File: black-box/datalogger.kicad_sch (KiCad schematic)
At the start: 75 parts, among them J1 RJ12, J10 PROG, J14 PWR, J4 Micro_SD_Card_Det1, J6 USB_C_Receptacle_USB2.0_16P, SW1 SW_SPST, U4 STM32F103C8Tx, U5 AP63200WU, U6 SN65HVD256D, U7 AP2204K-ADJ, Y1 8M, Y2 32.768k

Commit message: black-box: update
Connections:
- net GND: now also J10.3 (Pin_3)
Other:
- note added: "2025/12/30"
- note removed: "2025/12/25"
- moved on the sheet: C15, C16, C17, JP1, R21, R22, R5, TP11, TP12, TP13, TP14, U6

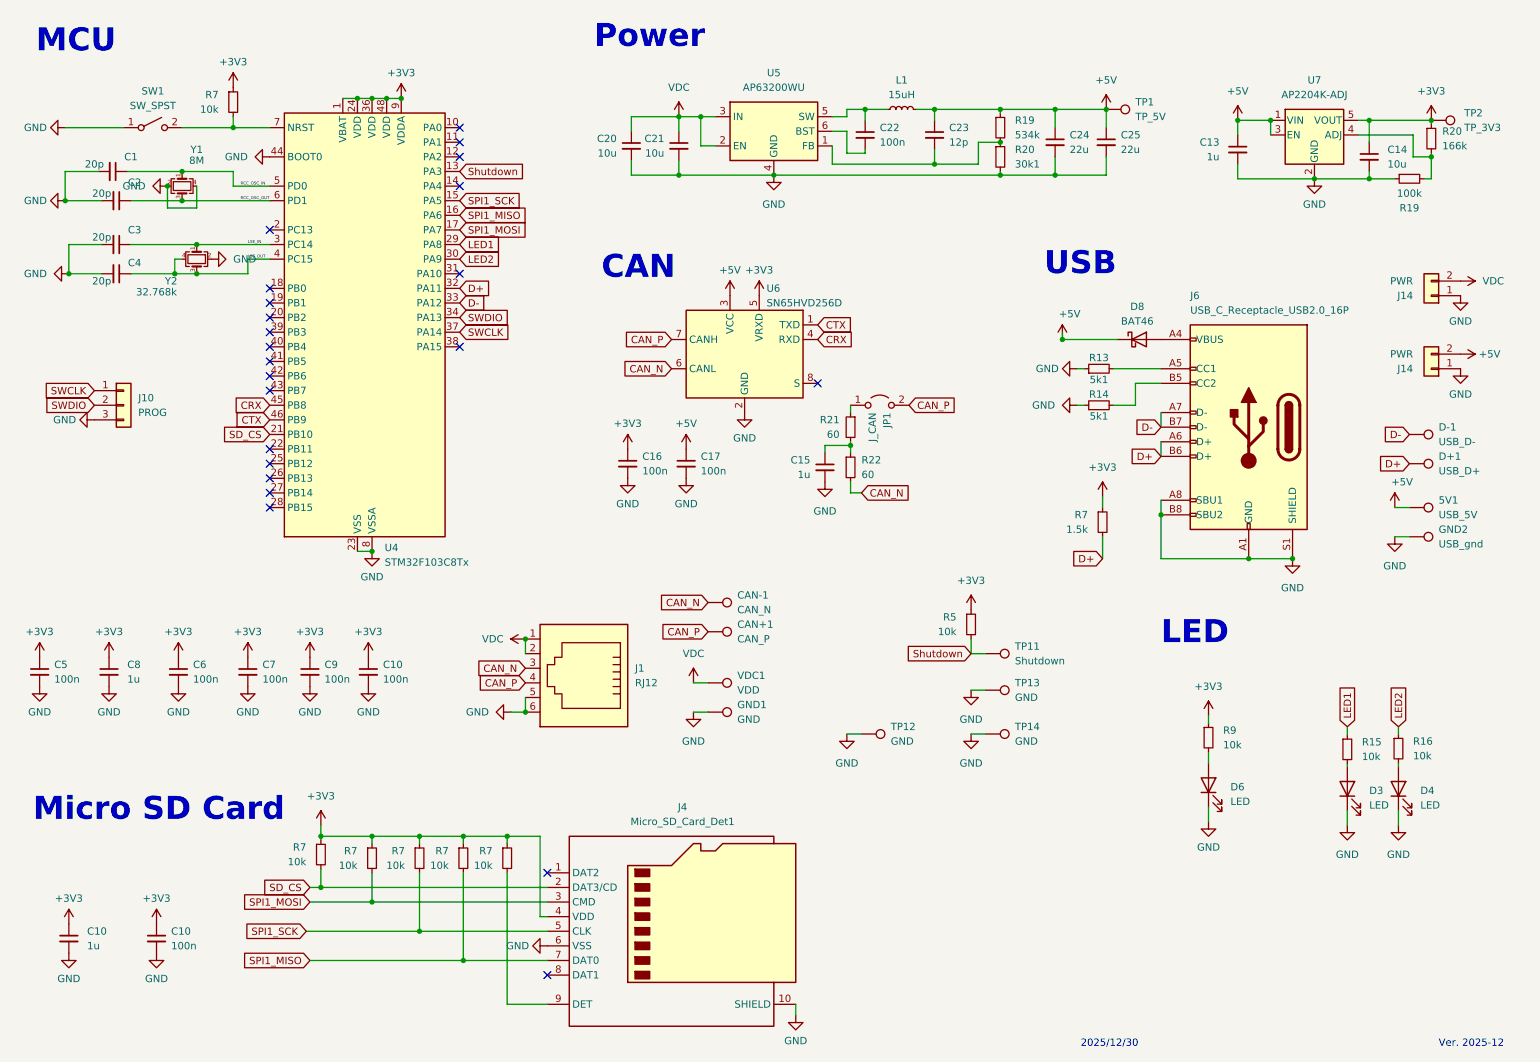
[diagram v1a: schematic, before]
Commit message: black-box: add WS2812 & 3D model
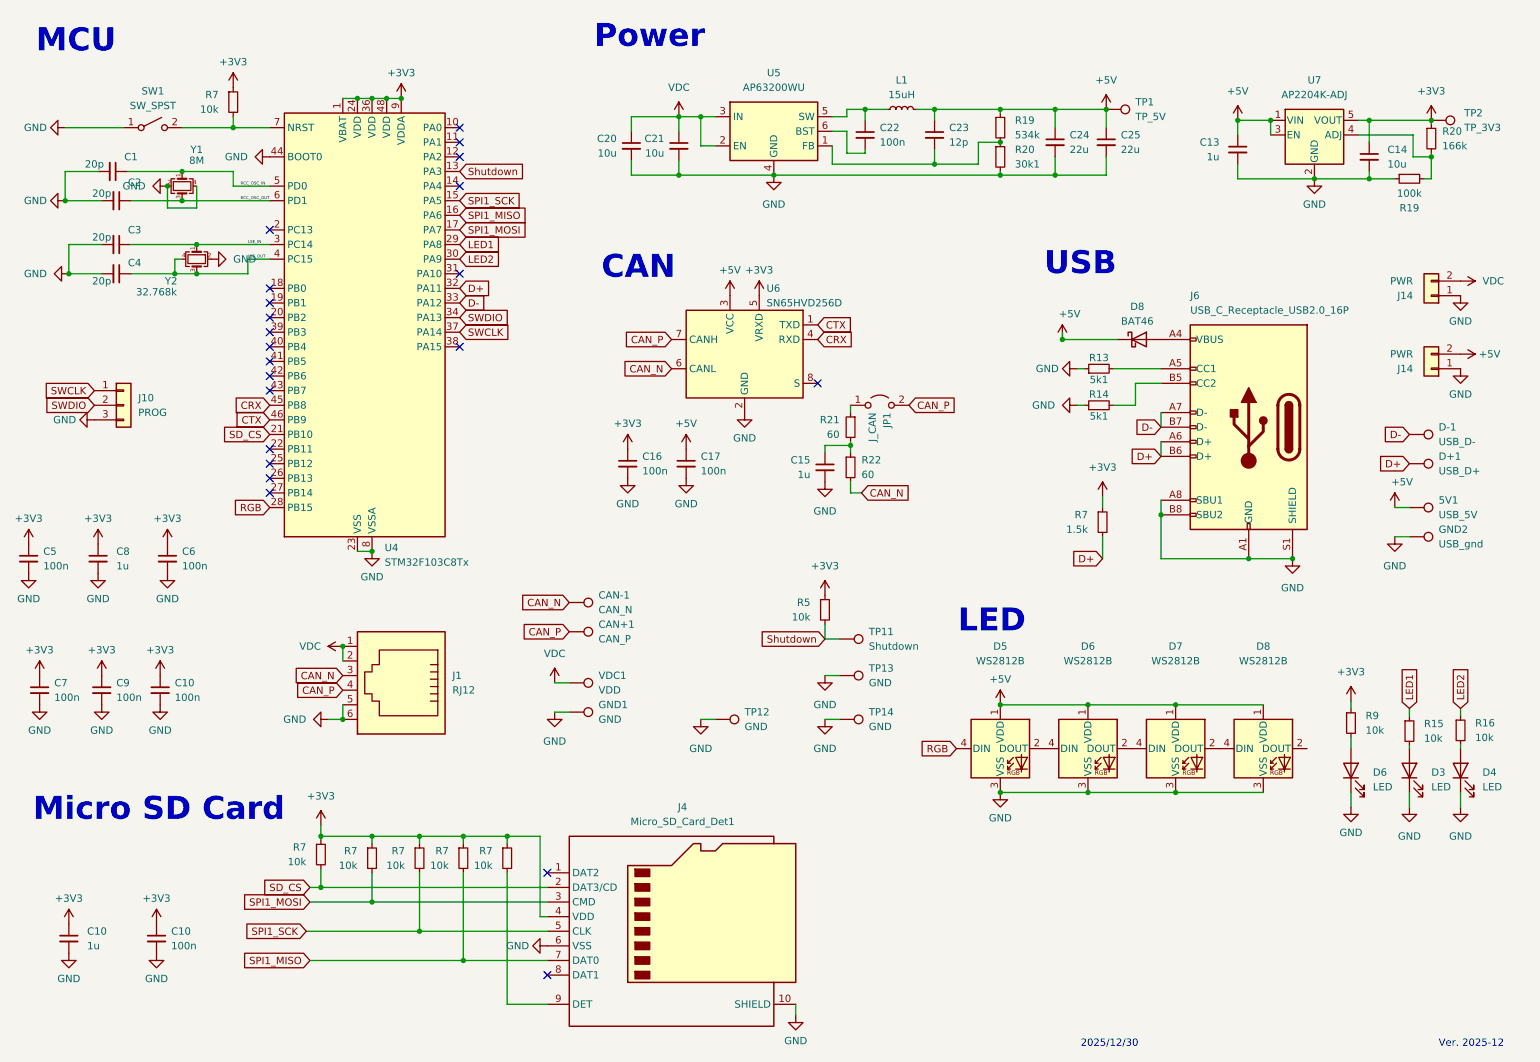
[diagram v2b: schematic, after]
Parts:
- added D5, D6, D7, D8: WS2812B, LED_SMD:LED_WS2812B_PLCC4_5.0x5.0mm_P3.2mm, symbol LED:WS2812B
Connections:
- net +5V: now also D5.1 (VDD), D6.1 (VDD), D7.1 (VDD), D8.1 (VDD)
- net GND: now also D5.3 (VSS), D6.3 (VSS), D7.3 (VSS), D8.3 (VSS)
- net RGB: now reaches U4.28 (PB15)
- net RGB: now also D5.4 (DIN)
- new net: D5.2 (DOUT), D6.4 (DIN)
- new net: D7.2 (DOUT), D8.4 (DIN)
- new net: D6.2 (DOUT), D7.4 (DIN)
- no-connect marks 23 -> 22
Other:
- moved on the sheet: C10, C5, C6, C7, C8, C9, CAN+1, CAN-1, D3, D4, D6, GND1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

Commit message: V2026.01: fix: USB pin and some issues
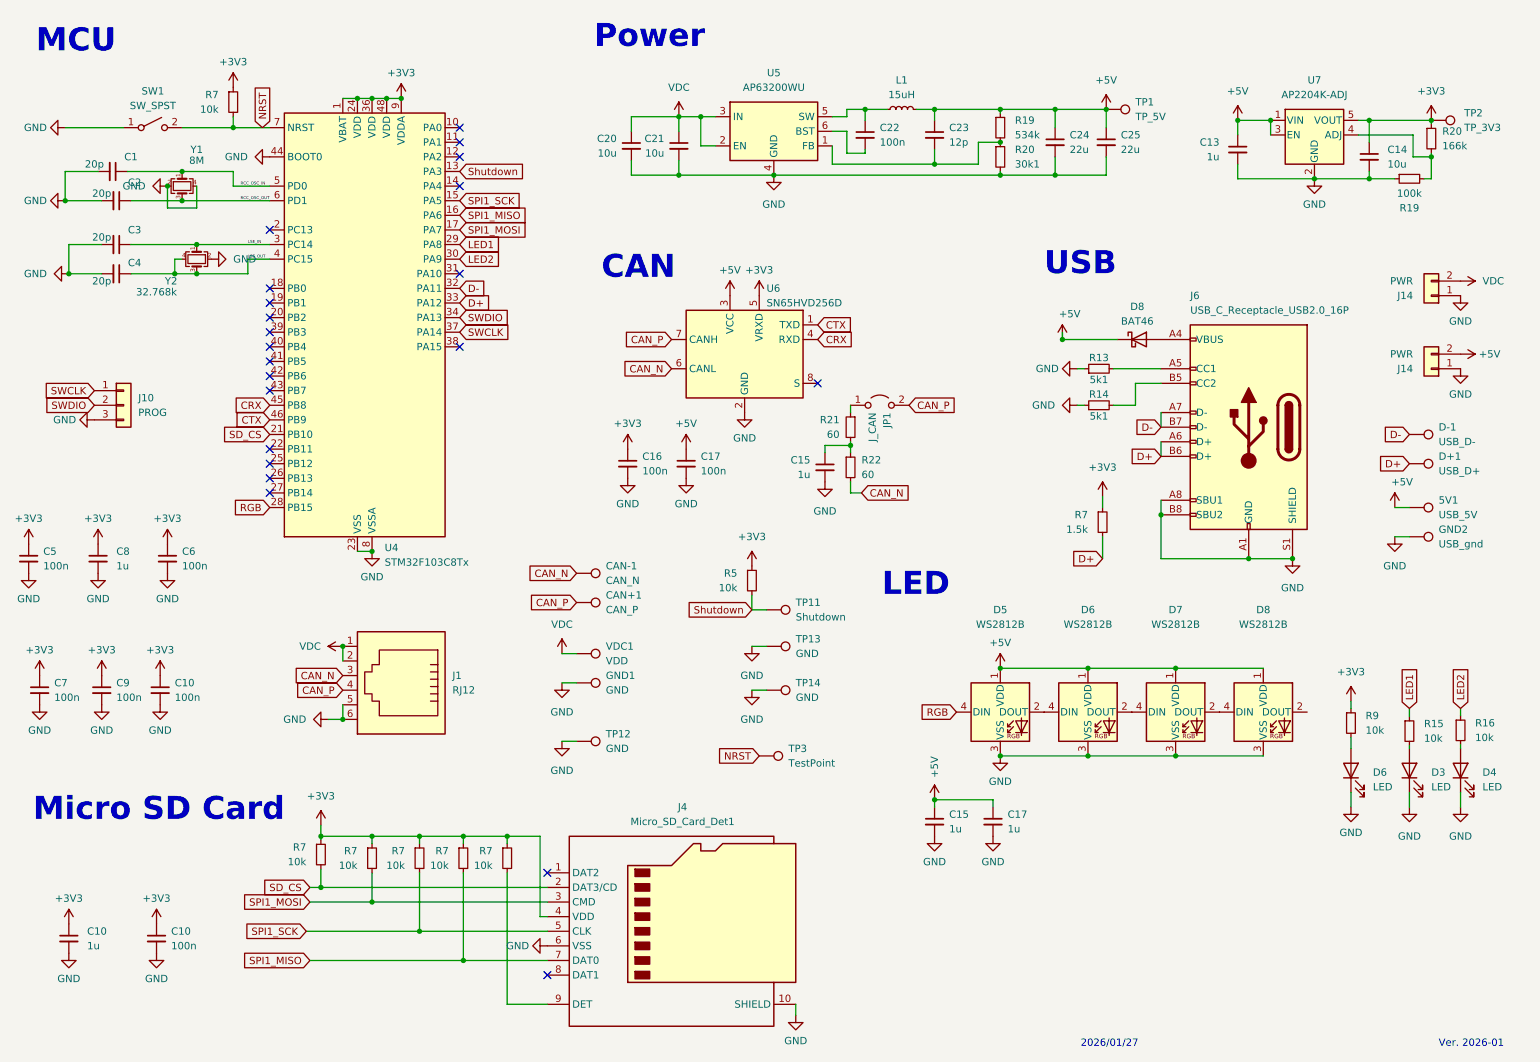
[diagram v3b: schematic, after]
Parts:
- added C15, C17: 1u, Capacitor_SMD:C_0805_2012Metric, symbol Device:C_Small
- added TP3: TestPoint, TestPoint:TestPoint_THTPad_D1.5mm_Drill0.7mm, symbol Connector:TestPoint
- C10, C13, C15, C8: footprint Capacitor_SMD:C_0603_1608Metric -> Capacitor_SMD:C_0805_2012Metric
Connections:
- net +5V: now also C15.1, C17.1
- net D+: now also U4.33 (PA12); no longer U4.32 (PA11)
- net D-: now also U4.32 (PA11); no longer U4.33 (PA12)
- net GND: now also C15.2, C17.2
- net NRST: now reaches R7.2, SW1.2 (B), U4.7 (NRST)
- net NRST: now also TP3.1
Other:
- note added: "2026/01/27"
- note added: "Ver. 2026-01"
- note removed: "2025/12/30"
- note removed: "Ver. 2025-12"
- moved on the sheet: CAN+1, CAN-1, D5, D6, D7, D8, GND1, R5, TP11, TP12, TP13, TP14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

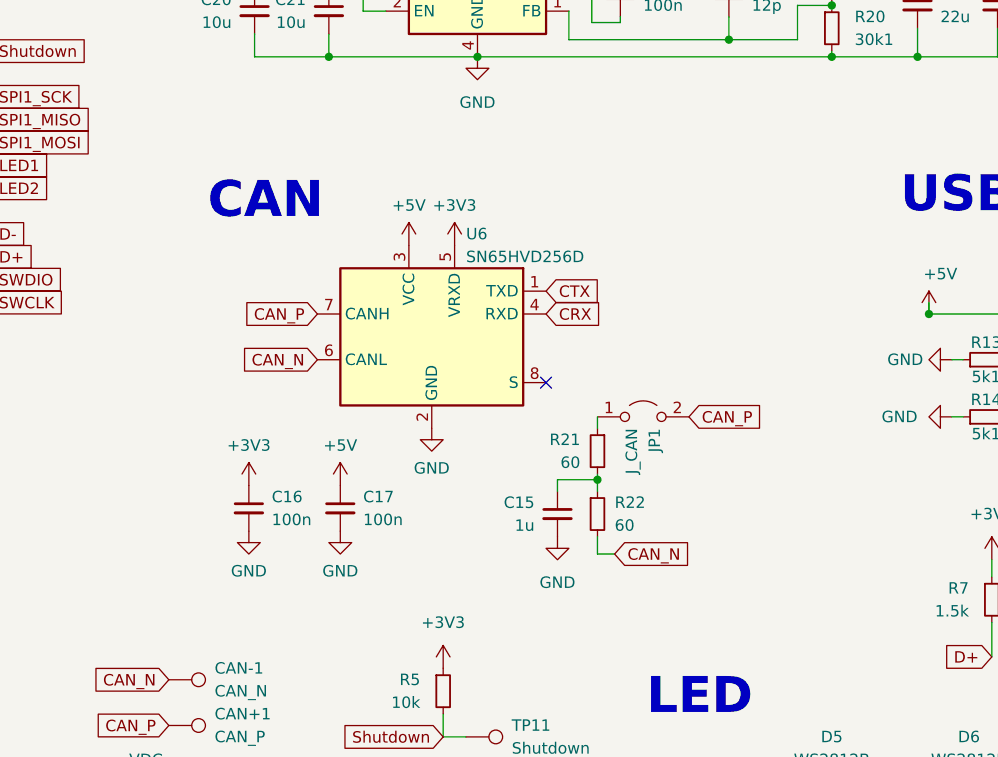
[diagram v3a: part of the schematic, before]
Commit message: feat: add can esd
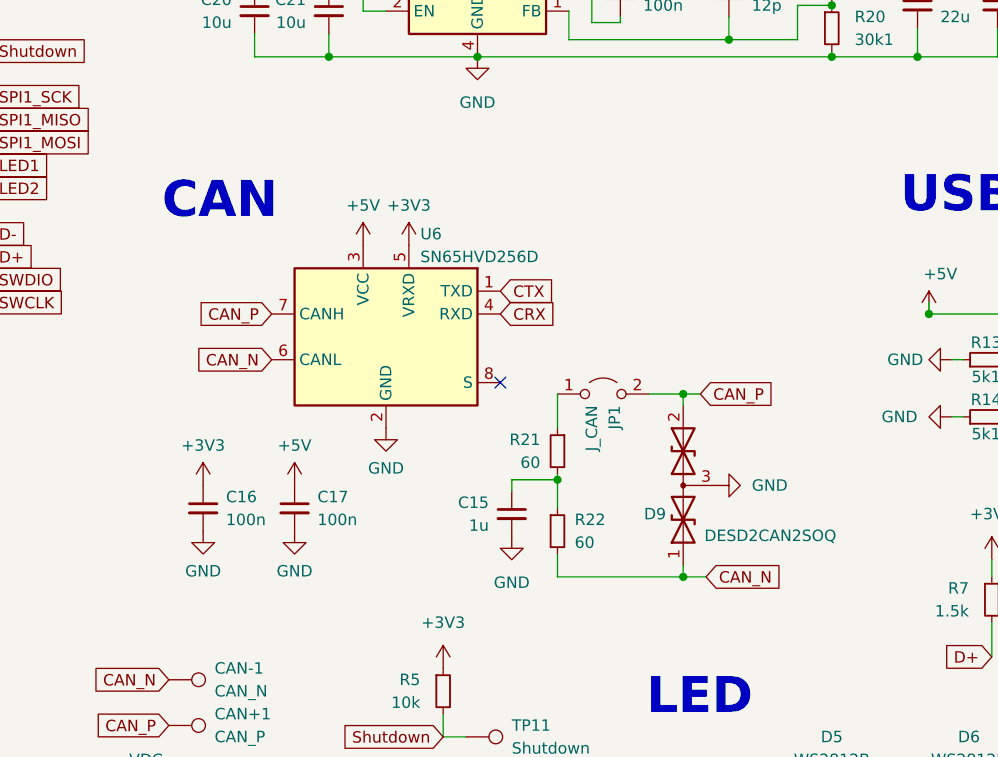
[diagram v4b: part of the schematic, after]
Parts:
- added D9: DESD2CAN2SOQ, Package_TO_SOT_SMD:TSOT-23, symbol Device:D_TVS_Dual_AAC
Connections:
- net CAN_N: now also D9.1 (A1)
- net CAN_P: now also D9.2 (A2)
- net GND: now also D9.3 (common)
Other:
- moved on the sheet: C15, C16, C17, JP1, R21, R22, U6

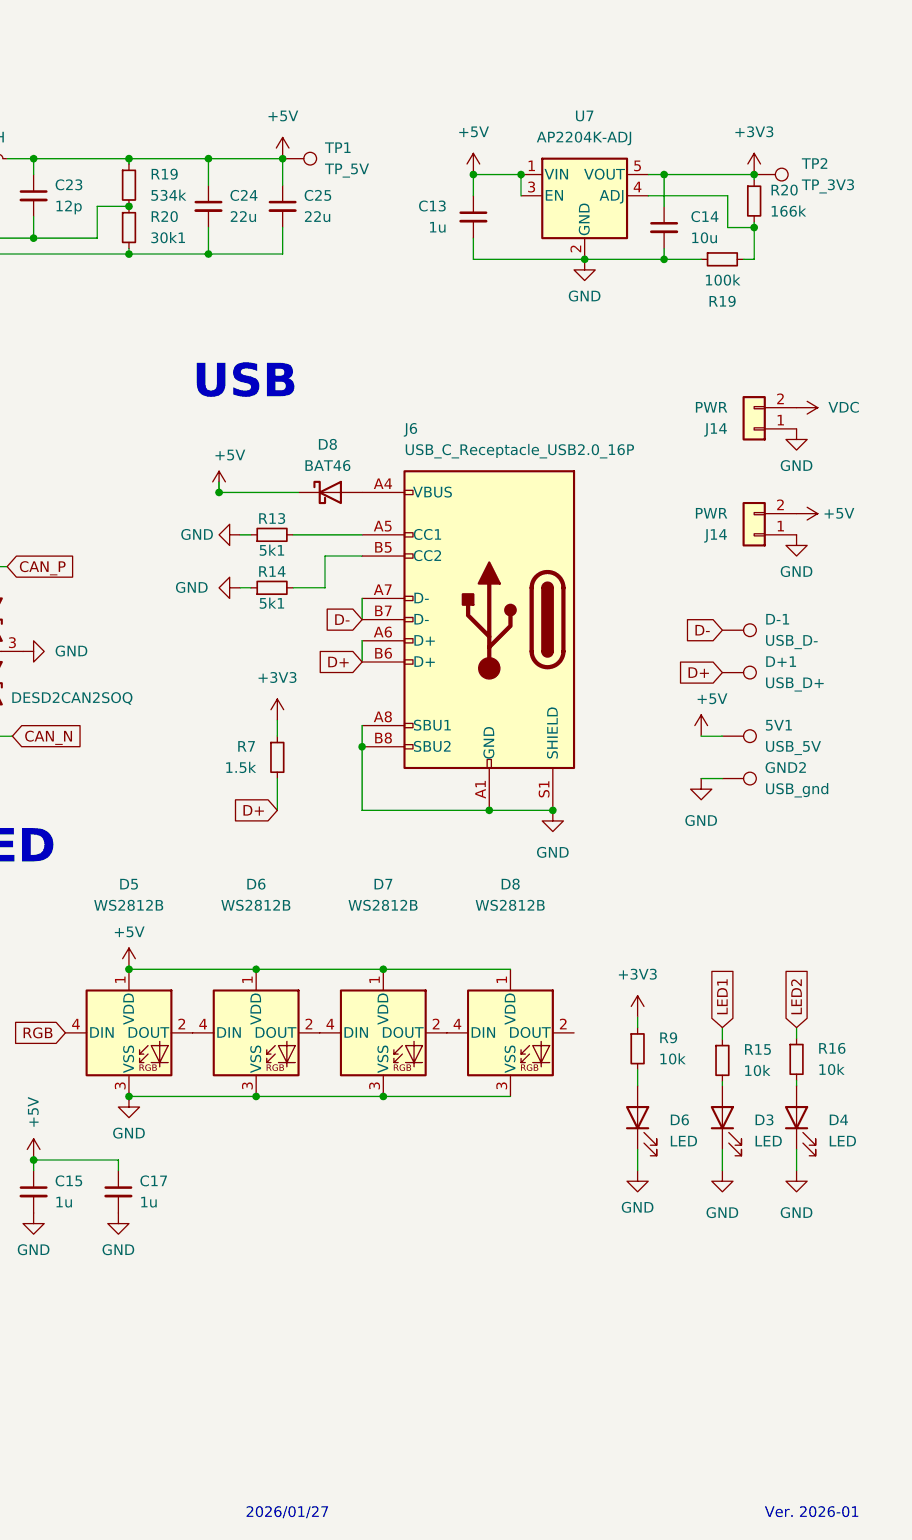
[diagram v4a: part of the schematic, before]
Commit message: update datalogger buck converter
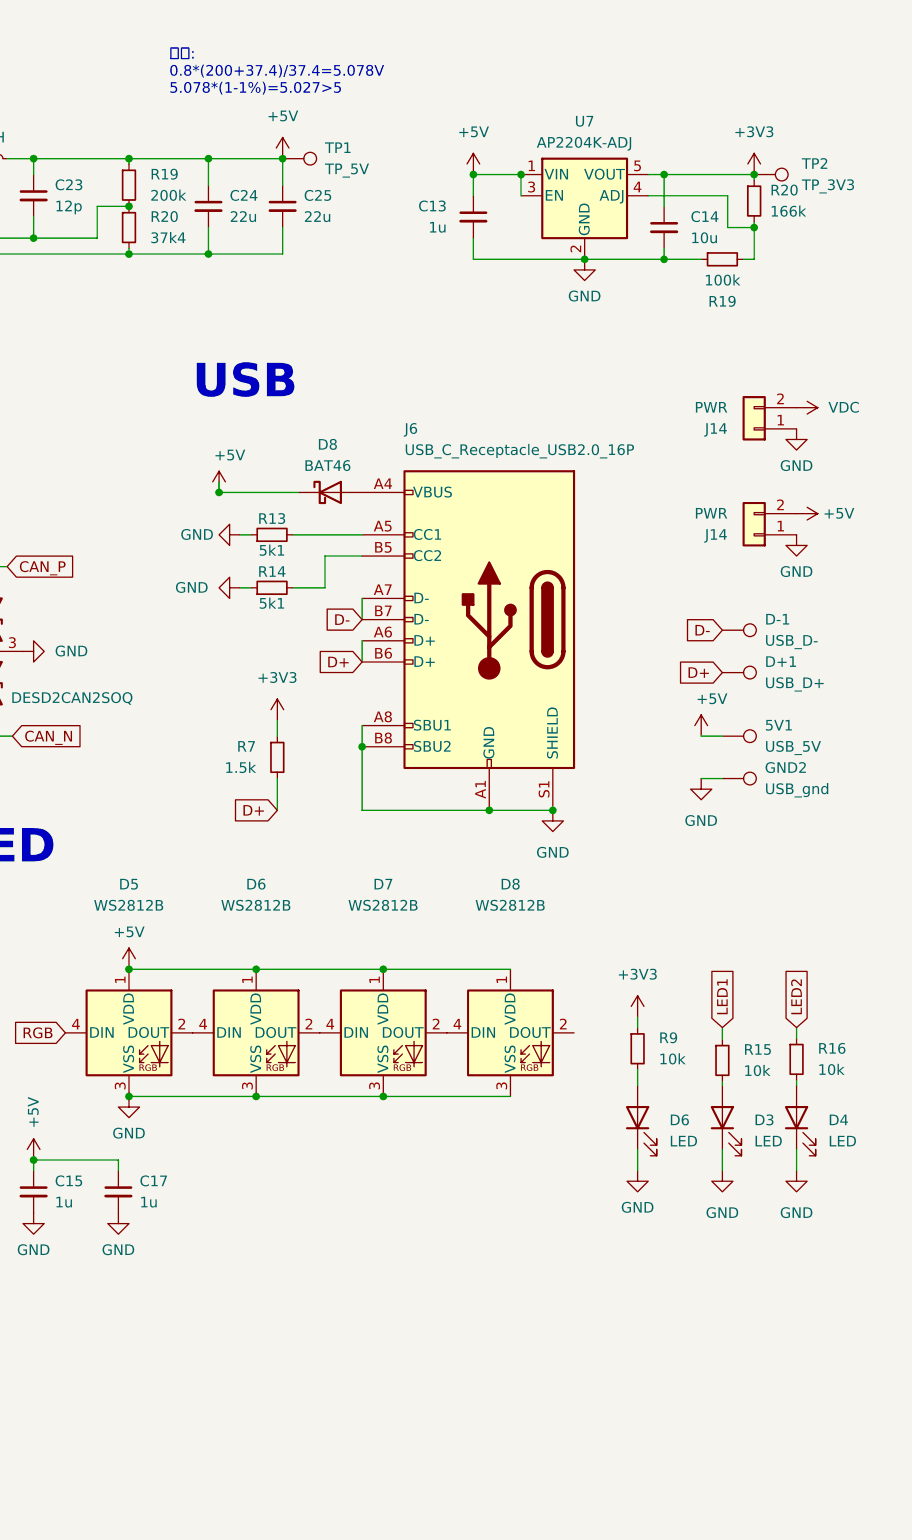
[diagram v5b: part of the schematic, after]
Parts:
- R19: value 534k -> 200k
- R20: value 30k1 -> 37k4
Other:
- note added: "輸出: 0.8*(200+37.4)/37.4=5.078V 5.078*(1-1%)=5.027>5"
- note removed: "2026/01/27"
- note removed: "Ver. 2026-01"
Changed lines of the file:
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@@
 	(generator_version "8.0")
 	(paper "A4")
+	(title_block
+		(date "2026-05-03")
+		(rev "Ver. 2026-05")
+		(comment 1 "buck converter part by 老百姓")
+	)
 	(junction
 		(at 202.565 42.545)
@@
 		)
 	)
-	(text "Ver. 2026-01"
+	(text "輸出:\n0.8*(200+37.4)/37.4=5.078V\n5.078*(1-1%)=5.027>5\n"
 		(exclude_from_sim no)
-		(at 269.24 194.31 0)
+		(at 197.866 20.828 0)
 		(effects
 			(font
 				(size 1.27 1.27)
 			)
-			(justify left bottom)
+			(justify left)
 		)
 	)
@@
 		)
 	)
-	(text "2026/01/27"
-		(exclude_from_sim no)
-		(at 207.01 194.31 0)
-		(effects
-			(font
-				(size 1.27 1.27)
-			)
-			(justify left bottom)
-		)
-	)
 	(text "CAN"
 		(exclude_from_sim no)
@@
 		(fields_autoplaced yes)
 		(property "Reference" "R20"
-			(at 195.58 38.1 0)
+			(at 195.58 38.0999 0)
 			(effects
 				(font
@@
 			)
 		)
-		(property "Value" "30k1"
-			(at 195.58 40.64 0)
+		(property "Value" "37k4"
+			(at 195.58 40.6399 0)
 			(effects
 				(font
@@
 		(fields_autoplaced yes)
 		(property "Reference" "R19"
-			(at 195.58 33.02 0)
+			(at 195.58 33.0199 0)
 			(effects
 				(font
@@
 			)
 		)
-		(property "Value" "534k"
-			(at 195.58 35.56 0)
+		(property "Value" "200k"
+			(at 195.58 35.5599 0)
 			(effects
 				(font
@@
 		(fields_autoplaced yes)
 		(property "Reference" "U7"
-			(at 247.65 26.035 0)
+			(at 247.65 26.67 0)
 			(effects
 				(font
@@
 		)
 		(property "Value" "AP2204K-ADJ"
-			(at 247.65 28.575 0)
+			(at 247.65 29.21 0)
 			(effects
 				(font
